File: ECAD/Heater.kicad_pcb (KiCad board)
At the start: 2 copper layers, 200 x 200 mm, 535 parts, among them J1 Conn_01x01_Female, J2 Conn_01x01_Female

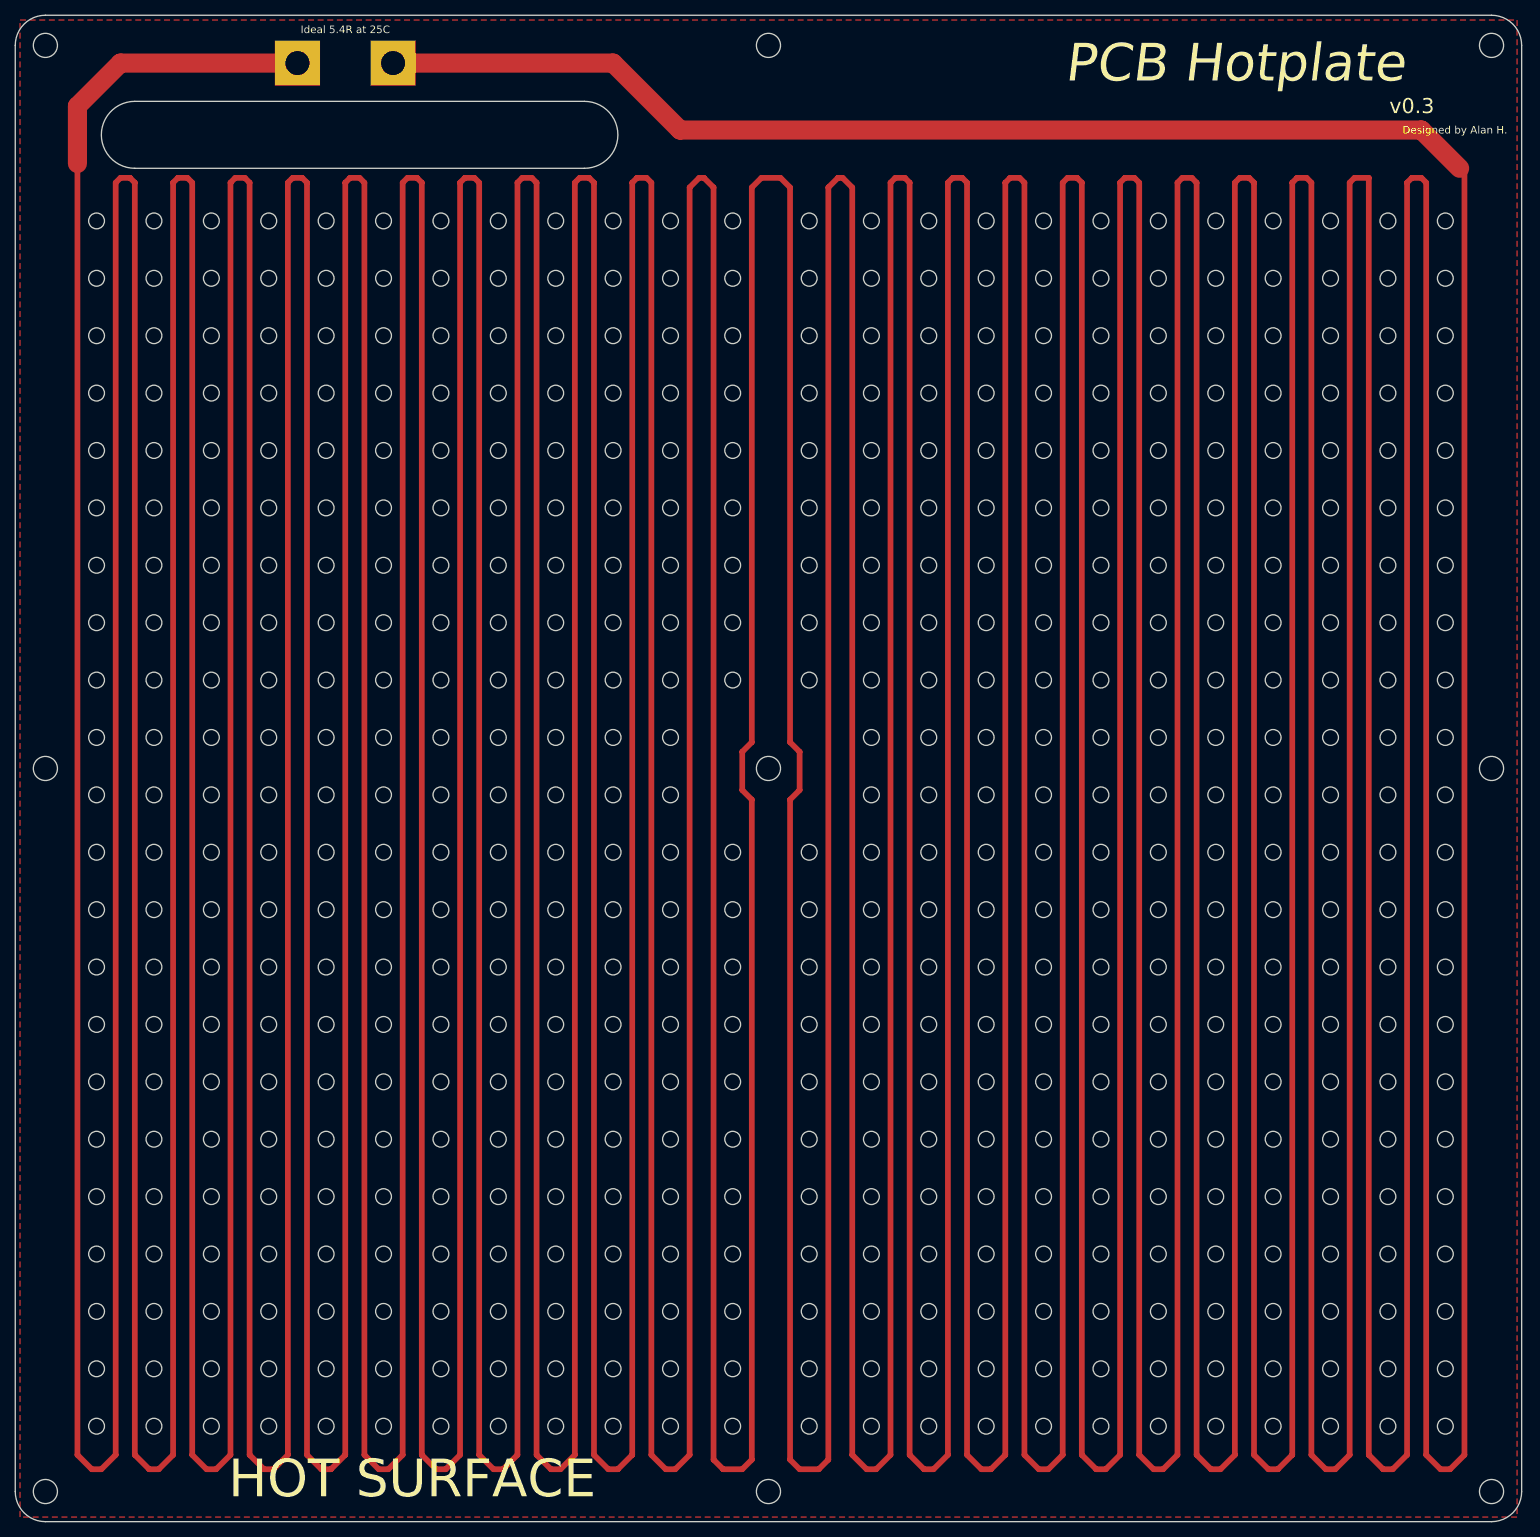
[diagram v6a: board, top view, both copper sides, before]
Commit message: Widen heater tracks
reduce actual resistance from 7ohm to 5ohm
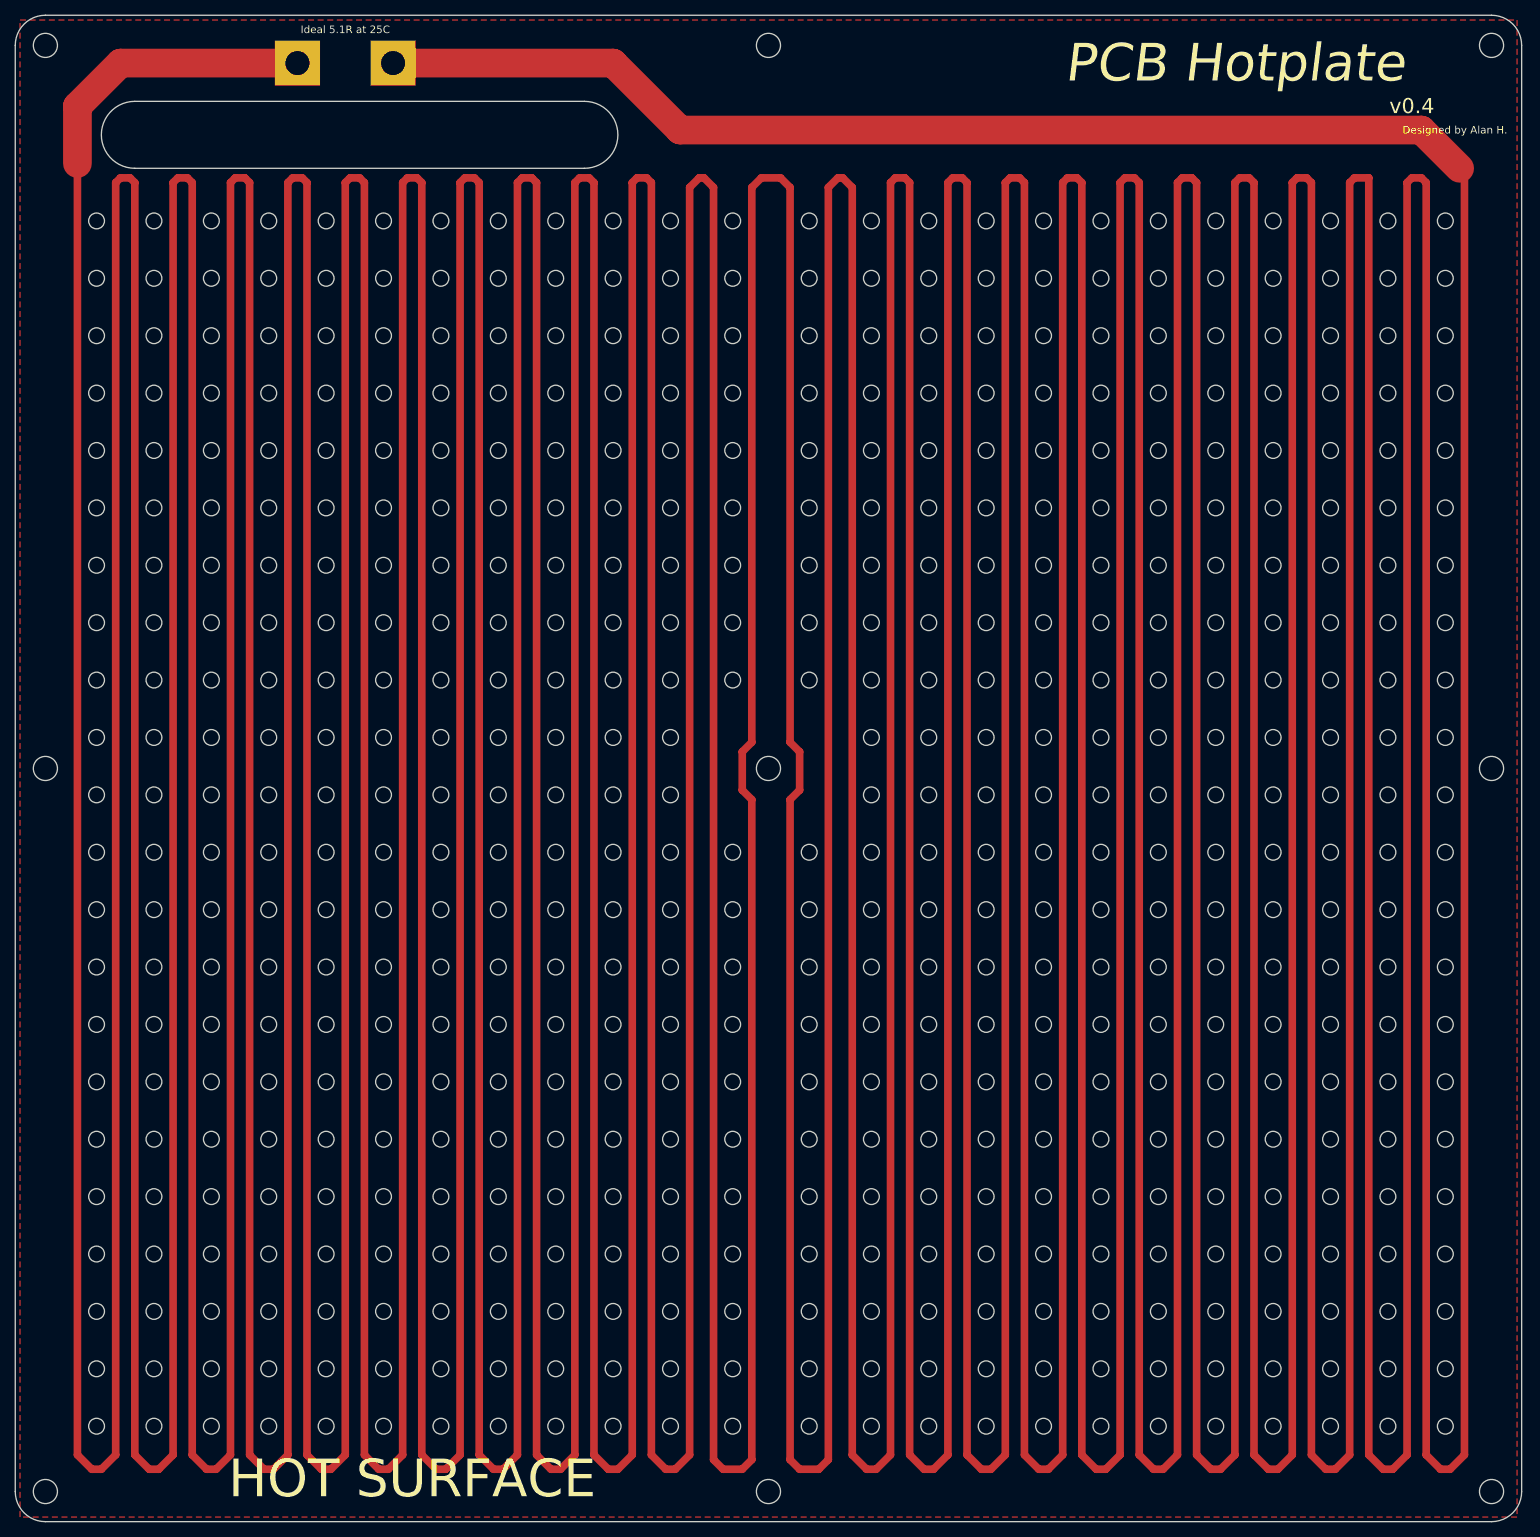
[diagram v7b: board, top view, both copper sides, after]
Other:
- board text added: "Ideal 5.1R at 25C"
- board text added: "v0.4"
- board text removed: "Ideal 5.4R at 25C"
- board text removed: "v0.3"

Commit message: Push v1.0 release version
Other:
- board text added: "v1.0"
- board text removed: "v0.4"
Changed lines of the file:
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@@
-(kicad_pcb (version 20171130) (host pcbnew "(5.1.10)-1")
+(kicad_pcb (version 20171130) (host pcbnew "(5.1.9)-1")
   (general
     (thickness 1.6)
@@
       (usegerberattributes true)
       (usegerberadvancedattributes true)
-      (creategerberjobfile false)
+      (creategerberjobfile true)
       (excludeedgelayer true)
       (linewidth 0.100000)
@@
     (effects (font (size 1 1) (thickness 0.15)))
   )
-  (gr_text v0.4 (at 195.58 22.225) (layer F.SilkS)
+  (gr_text v1.0 (at 195.58 22.225) (layer F.SilkS)
     (effects (font (size 2 2) (thickness 0.3)))
   )
